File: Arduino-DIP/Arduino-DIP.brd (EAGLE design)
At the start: 23.5 x 57.8 mm, 16 parts, among them IC1 ATMEGA 328, IC2 MCP1702-33, X1 16 MHz

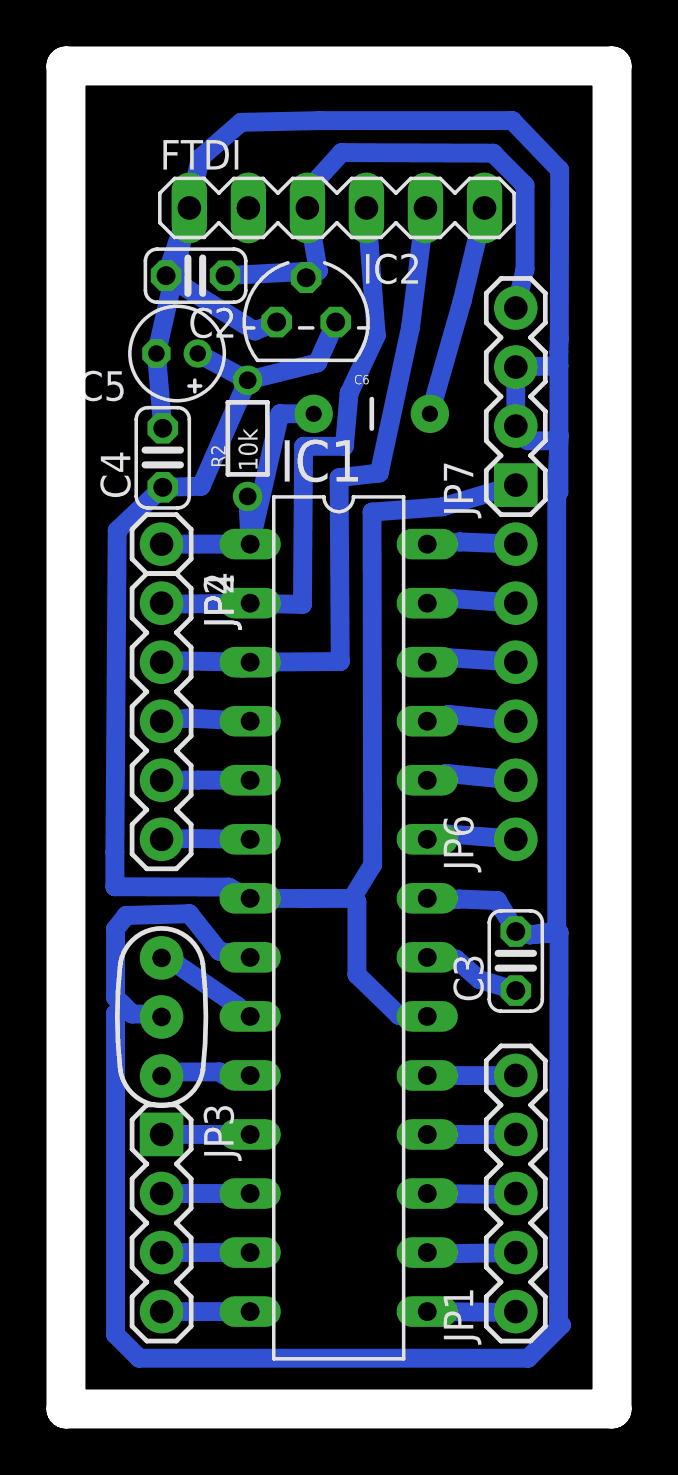
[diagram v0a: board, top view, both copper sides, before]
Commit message: added read me to SMD page
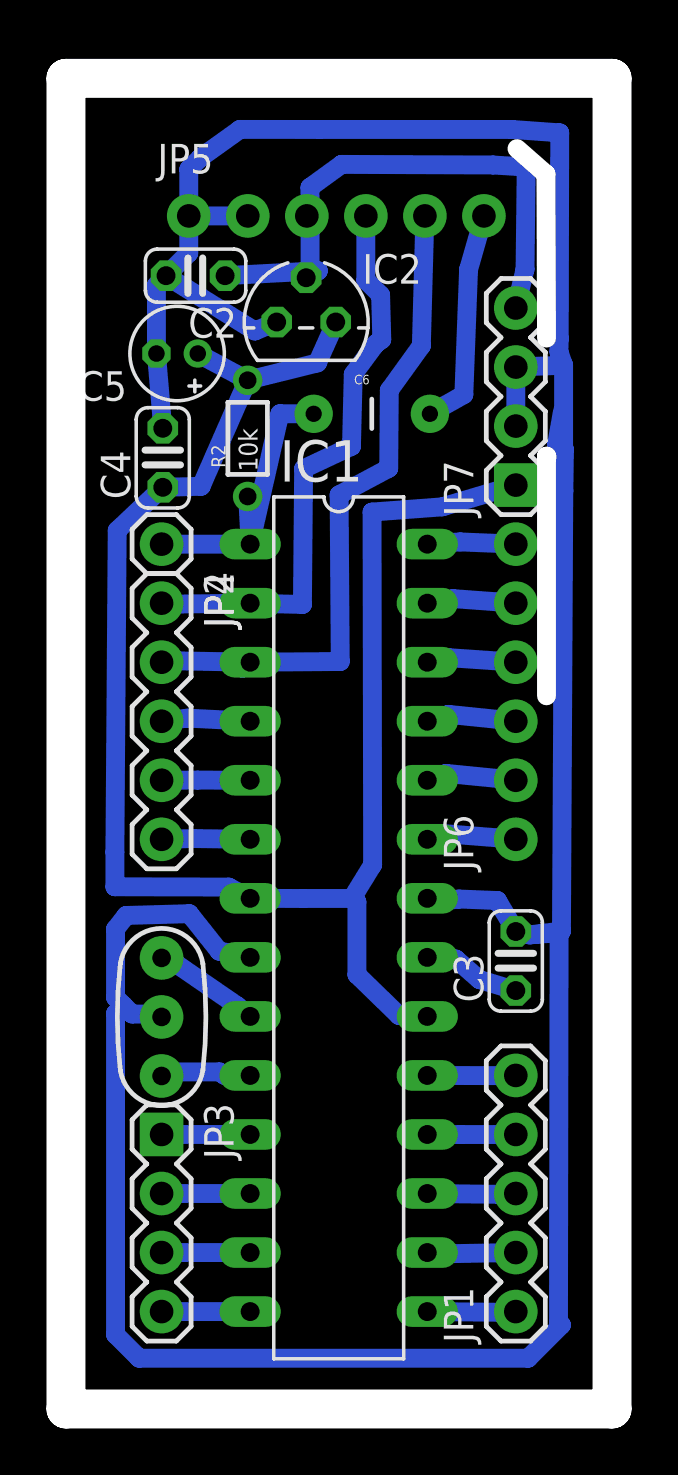
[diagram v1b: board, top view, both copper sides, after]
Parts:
- removed FTDI: FTDI, JeeLabs:MA06-1
- added JP5: (no value), SparkFun-Connectors:1X06_NO_SILK
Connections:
- net GND: now also JP5.1, JP5.2; no longer FTDI.1
- net N$20: now also JP5.6; no longer FTDI.6
- net PWR: now also JP5.3; no longer FTDI.3
- net RXD: now also JP5.4; no longer FTDI.4
- net TXD: now also JP5.5; no longer FTDI.5
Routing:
- net GND: track 149.9 -> 150.5 mm
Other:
- board size 23.5 x 57.8 mm -> 23.5 x 57.3 mm
